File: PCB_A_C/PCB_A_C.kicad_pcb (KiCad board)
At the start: 2 copper layers, 18 parts, among them J1 Conn_01x08_Socket, J2 Conn_01x04, J3 Screw_Terminal_01x02, SW1 SW_Push, SW2 SW_Push, SW3 SW_Push, SW4 SW_Push, SW5 SW_Push, U1 DHT11, U2 MSP430G2553IN20, Y0 32kHz

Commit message: Routed PCB.
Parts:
- J1: value Conn_01x08_Socket -> Conn01x08
- moved SW1 41.0 mm to (171.5, 104.3)
- moved SW5 41.0 mm to (128.9, 104.3)
- moved SW2 20.6 mm to (160.8, 104.3)
- moved SW4 20.5 mm to (139.5, 104.3)
- moved J1 17.8 mm to (143.5, 79.0), turned to 90 degrees
- moved D1 2.79 mm to (137.2, 78.7), turned to -90 degrees
- moved D2 2.79 mm to (167.6, 78.7), turned to -90 degrees
- moved Y0 1.31 mm to (161.0, 88.9)
- moved R1 1.04 mm to (153.7, 87.6), turned to 180 degrees
- moved SW3 0.51 mm to (150.2, 104.3)
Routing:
- net +BATT: track 0.00 -> 93.1 mm, vias 0 -> 1
- net RST: track 0.00 -> 46.6 mm, vias 0 -> 1
- net Net-(U2-P2.5/TA1.2): track 0.00 -> 41.8 mm, vias 0 -> 2
- net P2.2: track 0.00 -> 34.0 mm
- net P2.0: track 0.00 -> 31.8 mm, vias 0 -> 1
- net Net-(U2-UCA0TXD/UCA0SIMO/TA0.1/CA2/A2/P1.2): track 0.00 -> 31.2 mm
- net Net-(U2-TA0CLK/ACLK/CA0/A0/P1.0): track 0.00 -> 28.0 mm
- net Net-(U2-CAOUT/VREF-/VeREF-/CA3/A3/P1.3): track 0.00 -> 27.5 mm
- net Net-(U2-UCA0RXD/UCA0SOMI/TA0.0/CA1/A1/P1.1): track 0.00 -> 25.5 mm
- net P2.3: track 0.00 -> 22.7 mm
- net LIGHT: track 0.00 -> 20.7 mm
- net DIN: track 0.00 -> 15.6 mm
- net Net-(U2-P2.4/TA1.2): track 0.00 -> 14.6 mm
- net CE: track 0.00 -> 13.5 mm
- net Net-(BZ1--): track 0.00 -> 9.20 mm
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- added copper zone on B.Cu, net -BATT
- added copper zone on F.Cu, net -BATT
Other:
- board outline added: 55.9 x 44.4 mm

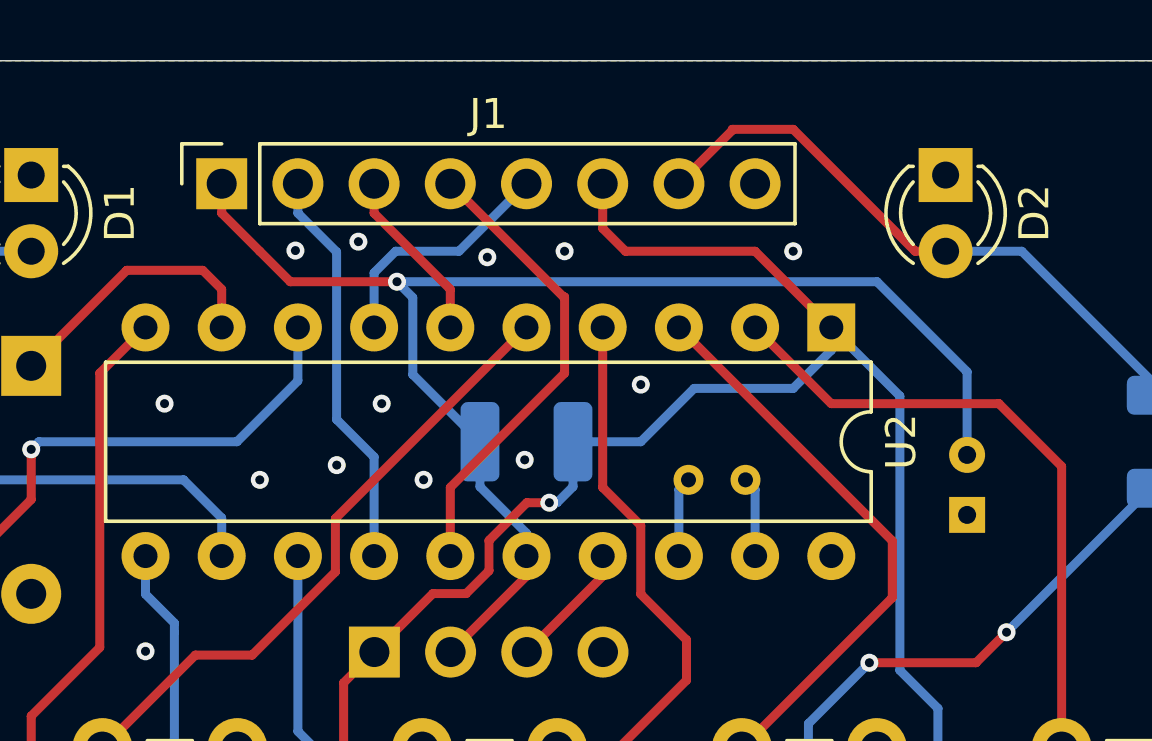
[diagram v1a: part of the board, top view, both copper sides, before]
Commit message: Corrected connector position on PCB.
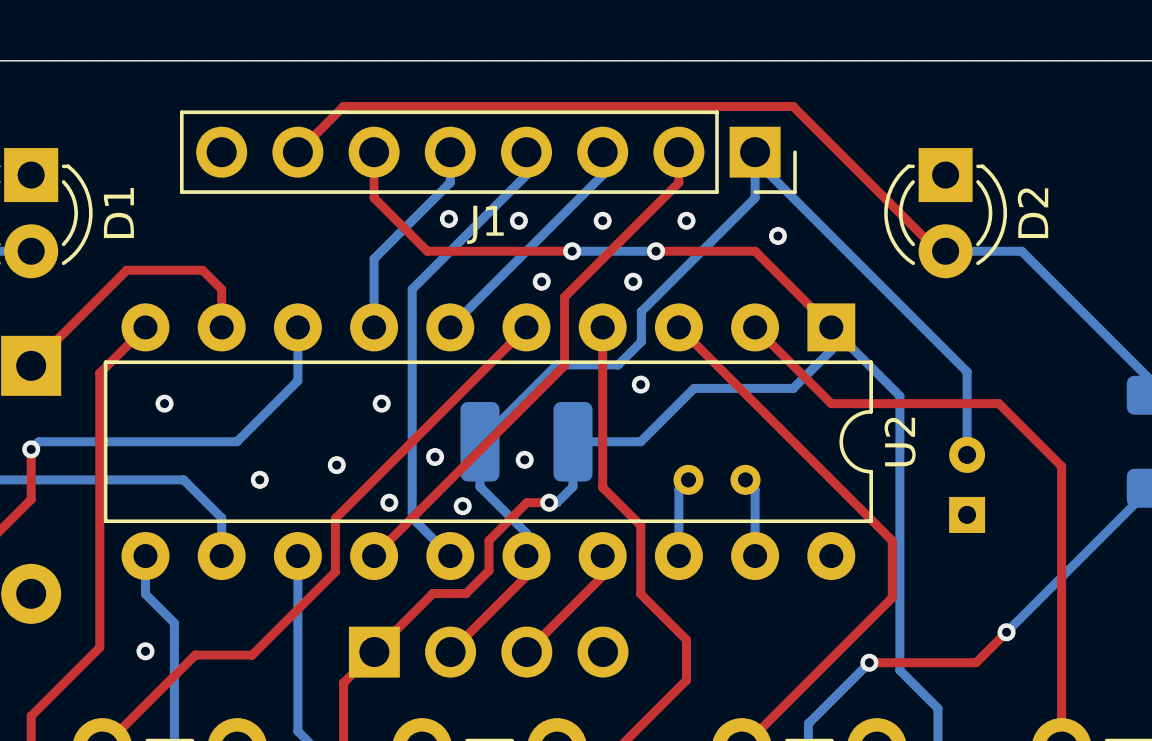
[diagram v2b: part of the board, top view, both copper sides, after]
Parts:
- moved J1 17.8 mm to (161.3, 78.0), turned to -90 degrees
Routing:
- net LIGHT: track 20.7 -> 33.6 mm
- net RST: track 46.6 -> 37.0 mm, vias 1 -> 0
- net +BATT: track 93.1 -> 101.1 mm, vias 1 -> 3
- net CE: track 13.5 -> 17.7 mm
- net DC: track 5.84 -> 7.95 mm
- net CLK: track 8.13 -> 6.89 mm
- net -BATT: vias 26 -> 30

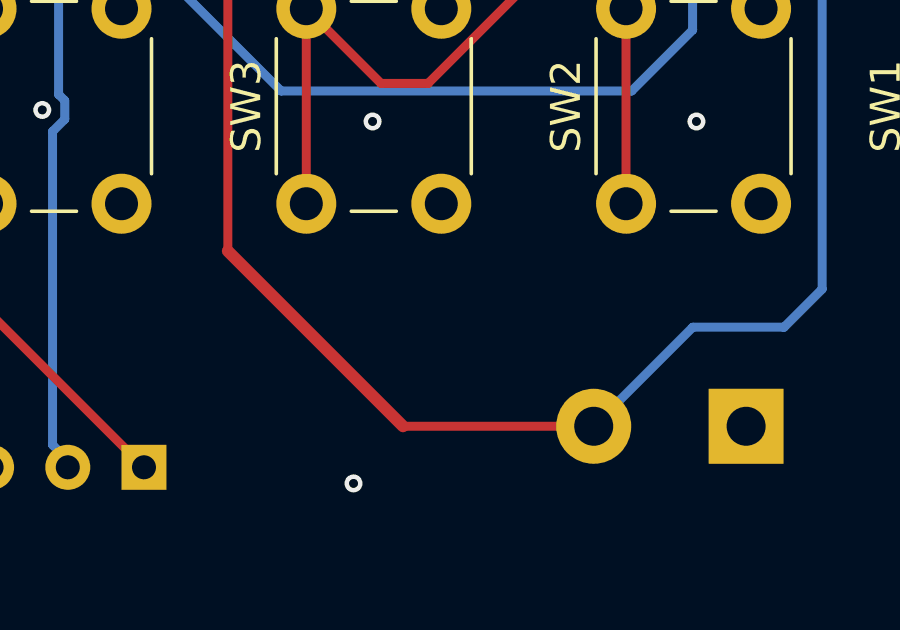
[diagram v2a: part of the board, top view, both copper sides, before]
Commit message: Implemented battery level monitor. Updated readme
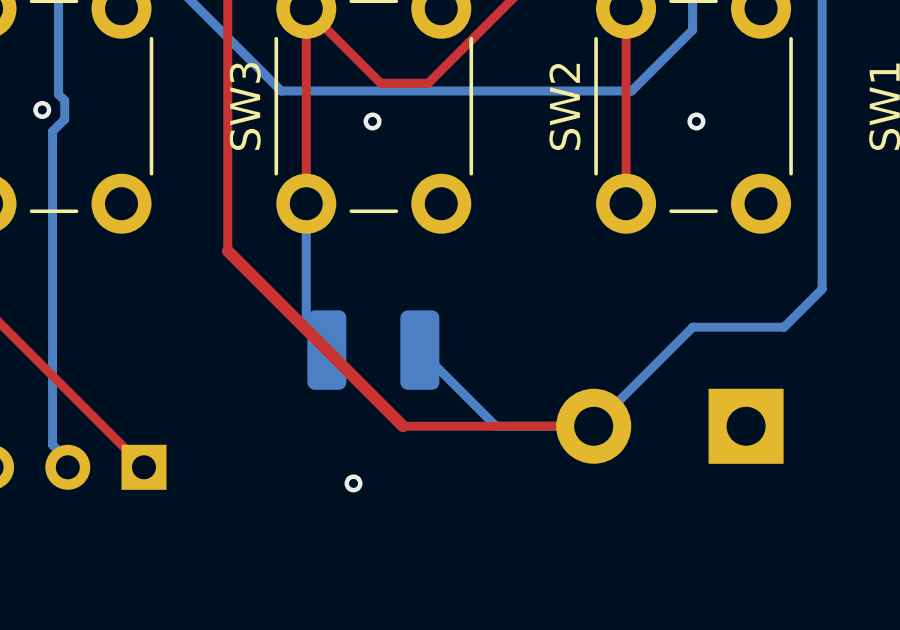
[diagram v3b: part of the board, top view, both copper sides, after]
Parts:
- added R4: 10k, Resistor_SMD:R_1210_3225Metric_Pad1.30x2.65mm_HandSolder, B.Cu at (152.4, 109.2)
- J1: value Conn01x08 -> Conn_01x08_Socket
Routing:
- net +BATT: track 101.1 -> 108.0 mm
- net Net-(U2-UCA0TXD/UCA0SIMO/TA0.1/CA2/A2/P1.2): track 31.2 -> 36.4 mm
